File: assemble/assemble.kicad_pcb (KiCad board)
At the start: 2 copper layers, 269.2 x 100.7 mm, 140 parts, among them J1 Conn_02x04_Odd_Even, SW1 SW_Push, SW10 SW_Push, SW11 SW_Push, SW12 SW_Push, SW13 SW_Push, SW14 SW_Push, SW15 SW_Push, SW16 SW_Push, SW17 SW_Push, SW18 SW_Push, SW19 SW_Push, SW2 SW_Push, SW20 SW_Push, SW21 SW_Push, SW22 SW_Push, SW23 SW_Push, SW24 SW_Push, SW25 SW_Push, SW26 SW_Push, SW27 SW_Push, SW28 SW_Push, SW29 SW_Push, SW3 SW_Push, SW30 SW_Push, SW31 SW_Push, SW32 SW_Push, SW33 SW_Push, SW34 SW_Push, SW35 SW_Push, SW36 SW_Push, SW37 SW_Push, SW38 SW_Push, SW39 SW_Push, SW4 SW_Push, SW40 SW_Push, SW41 SW_Push, SW42 SW_Push, SW43 SW_SPDT, SW44 SW_SPDT, SW45 RotaryEncoder_Switch, SW5 SW_Push, SW6 SW_Push, SW7 SW_Push, SW8 SW_Push, SW9 SW_Push, U1 XIAO-nRF52840-SMD, U2 XIAO-nRF52840-SMD

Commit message: wip: implement PCB
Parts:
- removed Ref** (x18): Val**, kbd_Hole:Mouse_Bite_Hole
- removed Ref** (x4): Val**, kbd_Hole:m2_Screw_Hole_EdgeCuts
- removed Ref** (x8): Val**, kbd_Hole:m3_Screw_Hole_EdgeCuts
- added BT3: Battery_Cell, kbd_Parts:Battery_AAA, F.Cu at (277.5, 30.0)
- added BT4: Battery_Cell, kbd_Parts:Battery_AAA, F.Cu at (26.0, 30.0)
- added C1: 0.01uF, kbd_Parts:Capacitor_1206, B.Cu at (241.4, 114.4)
- added C2: 0.01uF, kbd_Parts:Capacitor_1206, B.Cu at (241.4, 119.0)
- added C3: 0.01uF, kbd_Parts:Capacitor_1206, B.Cu at (62.3, 119.2)
- added C4: 0.01uF, kbd_Parts:Capacitor_1206, B.Cu at (62.3, 114.6)
- added J2: Conn_01x04, Connector_Wire:SolderWire-0.5sqmm_1x04_P4.6mm_D0.9mm_OD2.1mm, F.Cu at (128.8, 30.2)
- added J3: Conn_01x04, Connector_JST:JST_ZH_B4B-ZR_1x04_P1.50mm_Vertical, F.Cu at (166.2, 98.0)
- added J4: Conn_01x04, Connector_Wire:SolderWire-0.5sqmm_1x04_P4.6mm_D0.9mm_OD2.1mm, F.Cu at (175.2, 30.0)
- added R1: 10K, Resistor_SMD:R_0805_2012Metric_Pad1.20x1.40mm_HandSolder, B.Cu at (235.3, 114.4)
- added R2: 10K, Resistor_SMD:R_0805_2012Metric_Pad1.20x1.40mm_HandSolder, B.Cu at (235.4, 119.0)
- added R3: 10K, Resistor_SMD:R_0805_2012Metric_Pad1.20x1.40mm_HandSolder, B.Cu at (68.4, 119.2)
- added R4: 10K, Resistor_SMD:R_0805_2012Metric_Pad1.20x1.40mm_HandSolder, B.Cu at (68.4, 114.6)
- added SW46: RotaryEncoder_Switch, kbd_Parts:RotaryEncoder_EC12E, F.Cu at (64.8, 116.7)
- AE-XCL102D333CR-G1, AE-XCL102D333CR-G2, U1, U2: moved to F.Cu
- BT1, BT2: footprint Battery:BatteryHolder_Keystone_2460_1xAA -> kbd_Parts:Battery_AAA
- J1: value Conn_02x04_Odd_Even -> Conn_01x04; footprint Connector_PinSocket_2.54mm:PinSocket_2x04_P2.54mm_Vertical -> Connector_JST:JST_ZH_B4B-ZR_1x04_P1.50mm_Vertical; moved to B.Cu
- moved SW45 171.4 mm to (238.2, 116.6), turned to 0 degrees
- moved J1 120.3 mm to (137.7, 98.0)
- moved U2 117.5 mm to (168.8, 63.0), turned to 0 degrees
- moved U1 114.1 mm to (134.2, 63.0), turned to 0 degrees
- moved SW43 105.3 mm to (172.1, 24.6)
- moved SW44 101.6 mm to (131.3, 24.5)
- moved D1 88.5 mm to (132.9, 82.6), turned to -90 degrees
- moved SW4 88.3 mm to (189.0, 63.5), turned to 180 degrees
- moved SW5 88.3 mm to (189.0, 80.1), turned to 180 degrees
- moved SW6 88.3 mm to (189.0, 96.7), turned to 180 degrees
- moved D50 86.8 mm to (271.8, 60.8), turned to 180 degrees
- moved D2 86.8 mm to (130.2, 82.6), turned to -90 degrees
- moved D14 86.5 mm to (192.8, 69.4), turned to 0 degrees
- moved D15 86.3 mm to (193.0, 86.0), turned to 0 degrees
- moved D16 86.3 mm to (193.0, 102.6), turned to 0 degrees
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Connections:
- AE-XCL102D333CR-G1 pad 3: Net-(SW43-B) -> Net-(J3-Pin_3)
- AE-XCL102D333CR-G1 pad 5: BAT-R -> B-R
- AE-XCL102D333CR-G2 pad 3: Net-(SW44-B) -> Net-(J1-Pin_3)
- AE-XCL102D333CR-G2 pad 5: BAT-L -> B-L
- BT1 pad 1: B+R -> Net-(BT1-+)
- BT1 pad 2: BAT-R -> Net-(BT1--)
- BT2 pad 1: B+L -> Net-(BT2-+)
- BT2 pad 2: BAT-L -> Net-(BT2--)
- J1 pad 1: VCCR -> B+L
- J1 pad 2: GNDR -> B-L
- J1 pad 3: unconnected-(J1-Pin_3-Pad3) -> Net-(J1-Pin_3)
- J1 pad 4: unconnected-(J1-Pin_4-Pad4) -> Net-(AE-XCL102D333CR-G2-EN)
- SW43 pad 2: Net-(SW43-B) -> Net-(J4-Pin_4)
- SW43 pad 3: Net-(AE-XCL102D333CR-G1-EN) -> Net-(J4-Pin_3)
- SW44 pad 2: Net-(SW44-B) -> Net-(J2-Pin_4)
- SW44 pad 3: Net-(AE-XCL102D333CR-G2-EN) -> Net-(J2-Pin_3)
- SW45 pad A: RE1A -> Net-(R1-Pad2)
- SW45 pad B: RE1B -> Net-(R2-Pad2)
- SW45 pad C: GNDL -> GNDR
- U1 pad 16: BAT-L -> B-L
- U2 pad 1: PIN1R -> RE2A
- U2 pad 10: MISO -> PIN6R
- U2 pad 11: MOSI -> PIN7R
- U2 pad 16: BAT-R -> B-R
- U2 pad 17: CS -> unconnected-(U2-NFC1-Pad17)
- U2 pad 18: PIN7R -> unconnected-(U2-NFC2-Pad18)
- U2 pad 2: PIN2R -> RE2B
- U2 pad 5: PIN3R -> PIN1R
- U2 pad 6: PIN4R -> PIN2R
- U2 pad 7: PIN5R -> PIN3R
- U2 pad 8: PIN6R -> PIN4R
- U2 pad 9: SCK -> PIN5R
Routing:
- net B+L: track 281.0 -> 0.00 mm, vias 5 -> 0
- net PIN2R: track 238.9 -> 0.00 mm, vias 13 -> 0
- net Net-(D1-A): track 234.4 -> 0.00 mm, vias 20 -> 0
- net Net-(D26-A): track 231.6 -> 0.00 mm, vias 24 -> 0
- net Net-(D17-A): track 223.8 -> 0.00 mm, vias 16 -> 0
- net PIN3R: track 223.1 -> 0.00 mm, vias 14 -> 0
- net PIN4R: track 220.0 -> 0.00 mm, vias 11 -> 0
- net Net-(D18-A): track 216.1 -> 0.00 mm, vias 19 -> 0
- net Net-(D25-A): track 212.3 -> 0.00 mm, vias 20 -> 0
- net PIN1R: track 210.2 -> 0.00 mm, vias 16 -> 0
- net Net-(D10-A): track 205.7 -> 0.00 mm, vias 16 -> 0
- net B+R: track 193.4 -> 0.00 mm, vias 5 -> 0
- net Net-(AE-XCL102D333CR-G1-EN): track 192.0 -> 0.00 mm, vias 2 -> 0
- net Net-(SW43-B): track 187.1 -> 0.00 mm, vias 2 -> 0
- net BAT-L: track 173.2 -> 0.00 mm, vias 4 -> 0
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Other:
- board outline removed
- board text removed: "ON"
- board text removed: "ThingnusBall v1.0 designed by derui"

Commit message: fix: move pcb
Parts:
- moved D45 12.6 mm to (255.8, 87.8), turned to 0 degrees
- moved D46 12.6 mm to (255.4, 104.6), turned to 0 degrees
- moved J1 1.00 mm to (136.7, 98.0)
- moved D13 0.57 mm to (30.6, 106.2)
- moved D44 0.40 mm to (255.6, 71.4), turned to 0 degrees
- moved D10 0.27 mm to (178.0, 91.8)
- moved D34 0.18 mm to (170.0, 91.8)
- moved D18 0.13 mm to (175.3, 91.8)
- moved D26 0.07 mm to (172.7, 91.8)
- moved D5 0.05 mm to (178.0, 82.2)
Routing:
- net RE1A: track 0.00 -> 243.2 mm, vias 0 -> 9
- net Net-(D17-A): track 0.00 -> 241.0 mm, vias 0 -> 13
- net Net-(D1-A): track 0.00 -> 238.9 mm, vias 0 -> 16
- net RE1B: track 0.00 -> 215.8 mm, vias 0 -> 5
- net Net-(D10-A): track 0.00 -> 197.3 mm, vias 0 -> 8
- net PIN1L: track 0.00 -> 188.7 mm, vias 0 -> 9
- net PIN2L: track 0.00 -> 186.9 mm, vias 0 -> 5
- net Net-(D18-A): track 0.00 -> 183.9 mm, vias 0 -> 10
- net Net-(D26-A): track 0.00 -> 163.2 mm, vias 0 -> 8
- net PIN3L: track 0.00 -> 159.5 mm, vias 0 -> 7
- net Net-(D25-A): track 0.00 -> 155.0 mm, vias 0 -> 10
- net PIN4R: track 0.00 -> 153.0 mm, vias 0 -> 3
- net GNDL: track 0.00 -> 152.0 mm, vias 0 -> 4
- net PIN6R: track 0.00 -> 145.2 mm, vias 0 -> 5
- net RE2A: track 0.00 -> 145.0 mm, vias 0 -> 5
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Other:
- board outline added: 259.6 x 111.5 mm

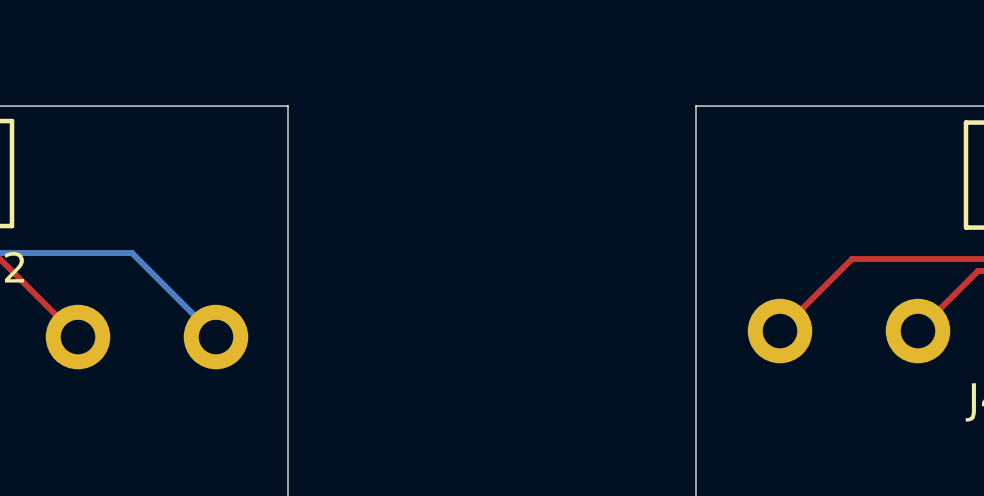
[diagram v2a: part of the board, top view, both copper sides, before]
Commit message: fix: add screw hole
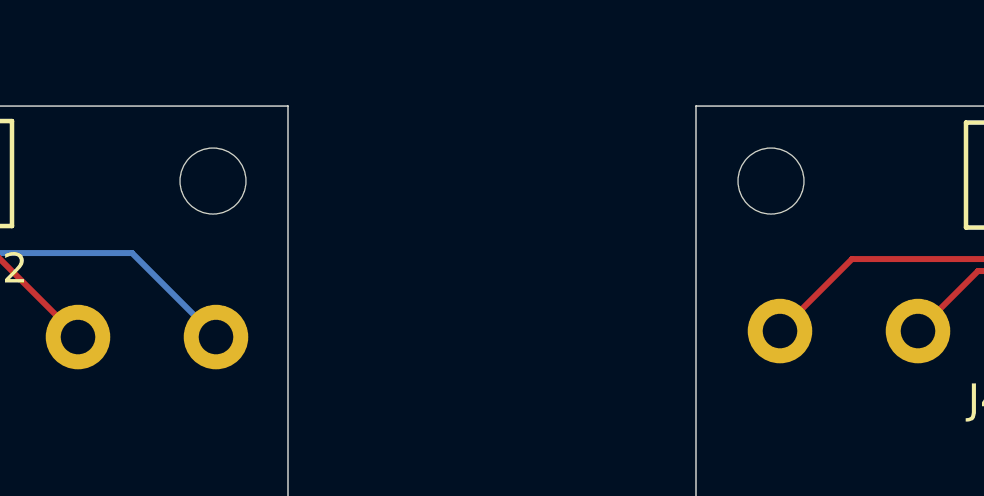
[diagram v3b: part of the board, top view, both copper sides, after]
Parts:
- added Ref**: Val**, kbd_Hole:m2_Screw_Hole, F.Cu at (142.5, 25.0)
- added Ref**: Val**, kbd_Hole:m2_Screw_Hole, F.Cu at (161.1, 25.0)
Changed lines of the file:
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@@
 		(embedded_fonts no)
 	)
+	(footprint "kbd_Hole:m2_Screw_Hole"
+		(layer "F.Cu")
+		(at 142.5 25)
+		(descr "Mounting Hole 2.2mm, no annular, M2")
+		(tags "mounting hole 2.2mm no annular m2")
+		(property "Reference" "Ref**"
+			(at 0 -3.2 0)
+			(layer "F.Fab")
+			(effects
+				(font
+					(size 1 1)
+					(thickness 0.15)
+				)
+			)
+		)
+		(property "Value" "Val**"
+			(at 0 3.2 0)
+			(layer "F.Fab")
+			(effects
+				(font
+					(size 1 1)
+					(thickness 0.15)
+				)
+			)
+		)
+		(property "Datasheet" ""
+			(at 0 0 0)
+			(layer "F.Fab")
+			(hide yes)
+			(effects
+				(font
+					(size 1.27 1.27)
+					(thickness 0.15)
+				)
+			)
+		)
+		(property "Description" ""
+			(at 0 0 0)
+			(layer "F.Fab")
+			(hide yes)
+			(effects
+				(font
+					(size 1.27 1.27)
+					(thickness 0.15)
+				)
+			)
+		)
+		(attr exclude_from_pos_files exclude_from_bom)
+		(fp_circle
+			(center 0 0)
+			(end 2.2 0)
+			(stroke
+				(width 0.15)
+				(type solid)
+			)
+			(fill no)
+			(layer "Cmts.User")
+		)
+		(fp_circle
+			(center 0 0)
+			(end 2.45 0)
+			(stroke
+				(width 0.05)
+				(type solid)
+			)
+			(fill no)
+			(layer "F.CrtYd")
+		)
+		(fp_text user "${REFERENCE}"
+			(at 0.3 0 0)
+			(layer "F.Fab")
+			(effects
+				(font
+					(size 1 1)
+					(thickness 0.15)
+				)
+			)
+		)
+		(pad "" np_thru_hole circle
+			(at 0 0)
+			(size 2.2 2.2)
+			(drill 2.2)
+			(layers "*.Cu" "*.Mask")
+		)
+		(embedded_fonts no)
+	)
 	(footprint "kbd_Parts:Diode_SMD"
 		(layer "F.Cu")
@@
 		(embedded_fonts no)
 	)
+	(footprint "kbd_Hole:m2_Screw_Hole"
+		(layer "F.Cu")
+		(at 161.1 25)
+		(descr "Mounting Hole 2.2mm, no annular, M2")
+		(tags "mounting hole 2.2mm no annular m2")
+		(property "Reference" "Ref**"
+			(at 0 -3.2 0)
+			(layer "F.Fab")
+			(effects
+				(font
+					(size 1 1)
+					(thickness 0.15)
+				)
+			)
+		)
+		(property "Value" "Val**"
+			(at 0 3.2 0)
+			(layer "F.Fab")
+			(effects
+				(font
+					(size 1 1)
+					(thickness 0.15)
+				)
+			)
+		)
+		(property "Datasheet" ""
+			(at 0 0 0)
+			(layer "F.Fab")
+			(hide yes)
+			(effects
+				(font
+					(size 1.27 1.27)
+					(thickness 0.15)
+				)
+			)
+		)
+		(property "Description" ""
+			(at 0 0 0)
+			(layer "F.Fab")
+			(hide yes)
+			(effects
+				(font
+					(size 1.27 1.27)
+					(thickness 0.15)
+				)
+			)
+		)
+		(attr exclude_from_pos_files exclude_from_bom)
+		(fp_circle
+			(center 0 0)
+			(end 2.2 0)
+			(stroke
+				(width 0.15)
+				(type solid)
+			)
+			(fill no)
+			(layer "Cmts.User")
+		)
+		(fp_circle
+			(center 0 0)
+			(end 2.45 0)
+			(stroke
+				(width 0.05)
+				(type solid)
+			)
+			(fill no)
+			(layer "F.CrtYd")
+		)
+		(fp_text user "${REFERENCE}"
+			(at 0.3 0 0)
+			(layer "F.Fab")
+			(effects
+				(font
+					(size 1 1)
+					(thickness 0.15)
+				)
+			)
+		)
+		(pad "" np_thru_hole circle
+			(at 0 0)
+			(size 2.2 2.2)
+			(drill 2.2)
+			(layers "*.Cu" "*.Mask")
+		)
+		(embedded_fonts no)
+	)
 	(footprint "kbd_Parts:Diode_SMD"
 		(layer "F.Cu")
@@
 	)
 	(gr_line
-		(start 281.6 22.5)
-		(end 158.6 22.5)
+		(start 22 22.5)
+		(end 22 37.5)
 		(stroke
 			(width 0.05)
@@
 	)
 	(gr_line
-		(start 280.8 50.3)
-		(end 158.2 50.3)
+		(start 22 22.5)
+		(end 145 22.5)
 		(stroke
 			(width 0.05)
@@
 	)
 	(gr_line
-		(start 158.6 22.5)
-		(end 158.6 37.5)
+		(start 22.2 124.8)
+		(end 22.2 50.3)
 		(stroke
 			(width 0.05)
@@
 	)
 	(gr_line
-		(start 158.2 114.6)
-		(end 158.2 50.3)
+		(start 22.2 124.8)
+		(end 117.6 124.8)
 		(stroke
 			(width 0.05)
@@
 	)
 	(gr_line
-		(start 133.6 134)
-		(end 144.8 114.6)
+		(start 117.6 124.8)
+		(end 133.6 134)
 		(stroke
 			(width 0.05)
@@
 	)
 	(gr_line
-		(start 144.8 50.3)
-		(end 22.2 50.3)
+		(start 133.6 134)
+		(end 144.8 114.6)
 		(stroke
 			(width 0.05)
@@
 	)
 	(gr_line
-		(start 145 37.5)
-		(end 22 37.5)
+		(start 144.8 50.3)
+		(end 22.2 50.3)
 		(stroke
 			(width 0.05)
@@
 	)
 	(gr_line
-		(start 117.6 124.8)
-		(end 133.6 134)
+		(start 144.8 114.6)
+		(end 144.8 50.3)
 		(stroke
 			(width 0.05)
@@
 	)
 	(gr_line
-		(start 158.2 114.6)
-		(end 169.2 134)
+		(start 145 22.5)
+		(end 145 37.5)
 		(stroke
 			(width 0.05)
@@
 	)
 	(gr_line
-		(start 22 22.5)
-		(end 145 22.5)
+		(start 145 37.5)
+		(end 22 37.5)
 		(stroke
 			(width 0.05)
@@
 	)
 	(gr_line
-		(start 22.2 124.8)
-		(end 117.6 124.8)
+		(start 158.2 114.6)
+		(end 158.2 50.3)
 		(stroke
 			(width 0.05)
@@
 	)
 	(gr_line
-		(start 22 22.5)
-		(end 22 37.5)
+		(start 158.2 114.6)
+		(end 169.2 134)
 		(stroke
 			(width 0.05)
@@
 	)
 	(gr_line
-		(start 280.8 124.8)
-		(end 280.8 50.3)
+		(start 158.6 22.5)
+		(end 158.6 37.5)
 		(stroke
 			(width 0.05)
@@
 	)
 	(gr_line
-		(start 281.6 22.5)
+		(start 158.6 37.5)
 		(end 281.6 37.5)
 		(stroke
@@
 	)
 	(gr_line
-		(start 145 22.5)
-		(end 145 37.5)
+		(start 169.2 134)
+		(end 185.4 124.8)
 		(stroke
 			(width 0.05)
@@
 	)
 	(gr_line
-		(start 22.2 124.8)
-		(end 22.2 50.3)
+		(start 280.8 50.3)
+		(end 158.2 50.3)
 		(stroke
 			(width 0.05)
@@
 	)
 	(gr_line
-		(start 169.2 134)
+		(start 280.8 124.8)
 		(end 185.4 124.8)
 		(stroke
@@
 	)
 	(gr_line
-		(start 158.6 37.5)
-		(end 281.6 37.5)
+		(start 280.8 124.8)
+		(end 280.8 50.3)
 		(stroke
 			(width 0.05)
@@
 	)
 	(gr_line
-		(start 144.8 114.6)
-		(end 144.8 50.3)
+		(start 281.6 22.5)
+		(end 158.6 22.5)
 		(stroke
 			(width 0.05)
@@
 	)
 	(gr_line
-		(start 280.8 124.8)
-		(end 185.4 124.8)
+		(start 281.6 22.5)
+		(end 281.6 37.5)
 		(stroke
 			(width 0.05)

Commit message: fix: add GND pattern
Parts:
- moved BT1 10.6 mm to (225.0, 40.6)
- moved BT3 10.6 mm to (277.0, 40.6)
- moved J4 10.6 mm to (174.7, 40.6)
- moved Ref** 10.6 mm to (160.6, 35.6)
- moved SW43 10.6 mm to (171.6, 35.1)
- moved BT2 10.6 mm to (77.9, 40.6)
- moved BT4 10.6 mm to (25.9, 40.6)
- moved Ref** 10.6 mm to (142.4, 35.6)
- moved SW44 10.6 mm to (131.2, 35.1)
- moved J2 10.6 mm to (128.7, 40.8)
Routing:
- net GNDR: vias 6 -> 12
- net GNDL: vias 4 -> 10
- added copper zone on B.Cu, net GNDL
- added copper zone on F.Cu, net GNDL
- added copper zone on B.Cu, net GNDR
- added copper zone on F.Cu, net GNDR
- added copper zone on B.Cu, net Net-(BT1--)
- added copper zone on F.Cu, net Net-(BT1--)
- added copper zone on B.Cu, net Net-(BT2--)
- added copper zone on F.Cu, net Net-(BT2--)
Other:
- board size 259.6 x 111.5 mm -> 259.2 x 100.9 mm
- board text added: "OFF"
- board text added: "ON"
